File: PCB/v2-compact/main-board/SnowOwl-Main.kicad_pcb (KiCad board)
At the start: 4 copper layers, 70 x 100 mm, 30 parts, among them J1 STACK_2x10, J20 USB-C, J30 microSD, J31 TFT_SPI, SW1 BTN_UP, SW2 BTN_DN, SW3 BTN_L, SW4 BTN_R, SW5 BTN_OK, U20 ESP32-S3-WROOM-1-N8, U21 AP7361C-3.3, U22 USBLC6-2SC6

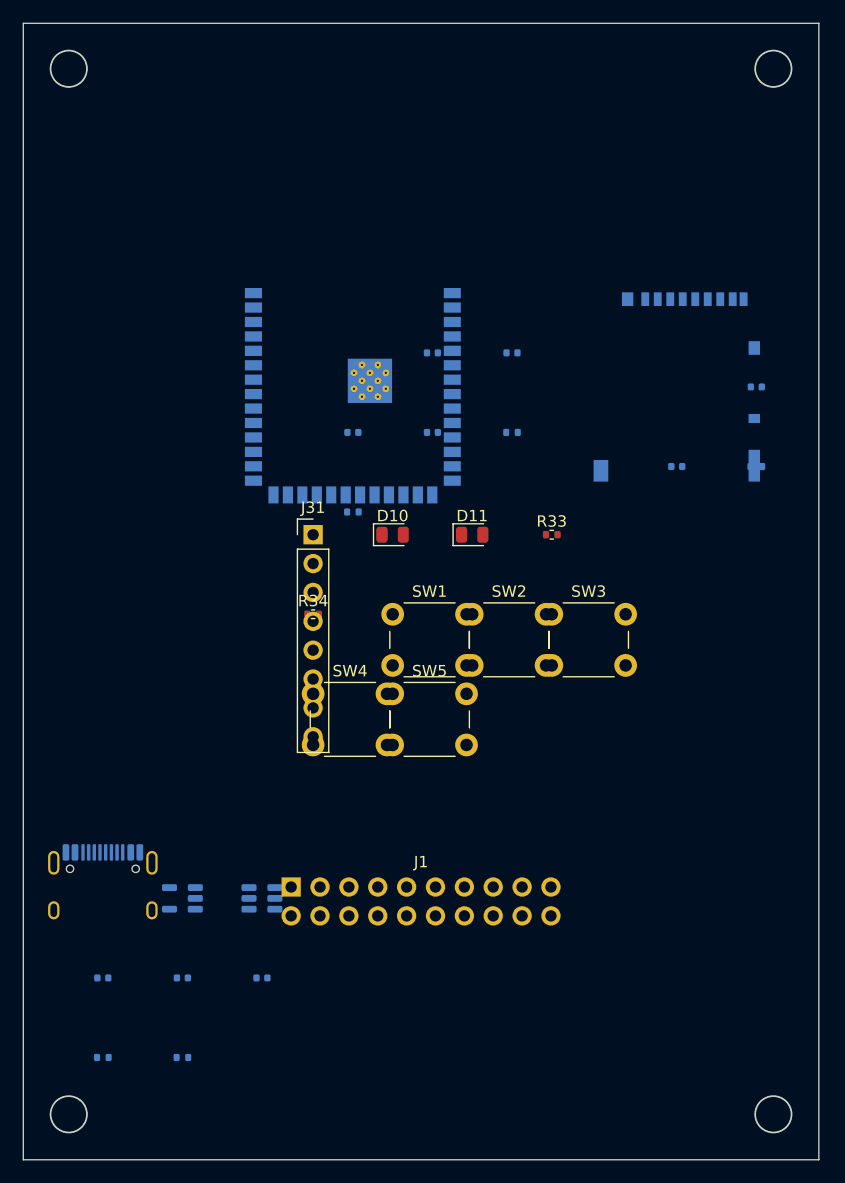
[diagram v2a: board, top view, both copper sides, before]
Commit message: PCB: intentional floorplan placement + 3D models + screen (both boards)
Reflow both boards to the PLACEMENT.md contract instead of a mechanical grid:
- Shield: radios north each behind its SMA, C5 (SPI master) centre with U.FL, the
  3 nRF24 on the back behind the QFN radios, MCP expander on the spine, PN532/flash/
  IR/iButton in their zones, J1 at the (53.57,106) datum, prog header off the crowded
  east edge. Main: pure-UI front (status LEDs, landscape TFT area, PlayStation D-pad
  SW1 up/SW2 down/SW3 left/SW4 right + SW5 select, J1 datum), all electronics on the
  back (S3 upper-centre with antenna to the edge, microSD east, power+USB-C south).
- Every support part anchored to the exact pin it shares a net with, then de-overlapped
  by spiralling out to the nearest clear spot inside the board, so decoupling hugs the
  power pins and crystals sit at the XTAL pins.
- Verified: 0 same-side courtyard overlaps, 0 cross-side through-hole collisions (new
  check that caught headers landing on back-side modules), every part in the outline.
- 3D models the renderer can find: C5 repointed to the Espressif model's absolute path,
  J1 given the KiCad 2x10 header body (rotated to match the horizontal pad layout).
- Draw the TFT display outline + label on the main front so the screen is visible.

Note: U9 (u-blox NEO) still renders as an outline - RF_GPS.3dshapes is absent from this
KiCad 3D pack; the footprint/courtyard are correct, only the cosmetic .step is missing.
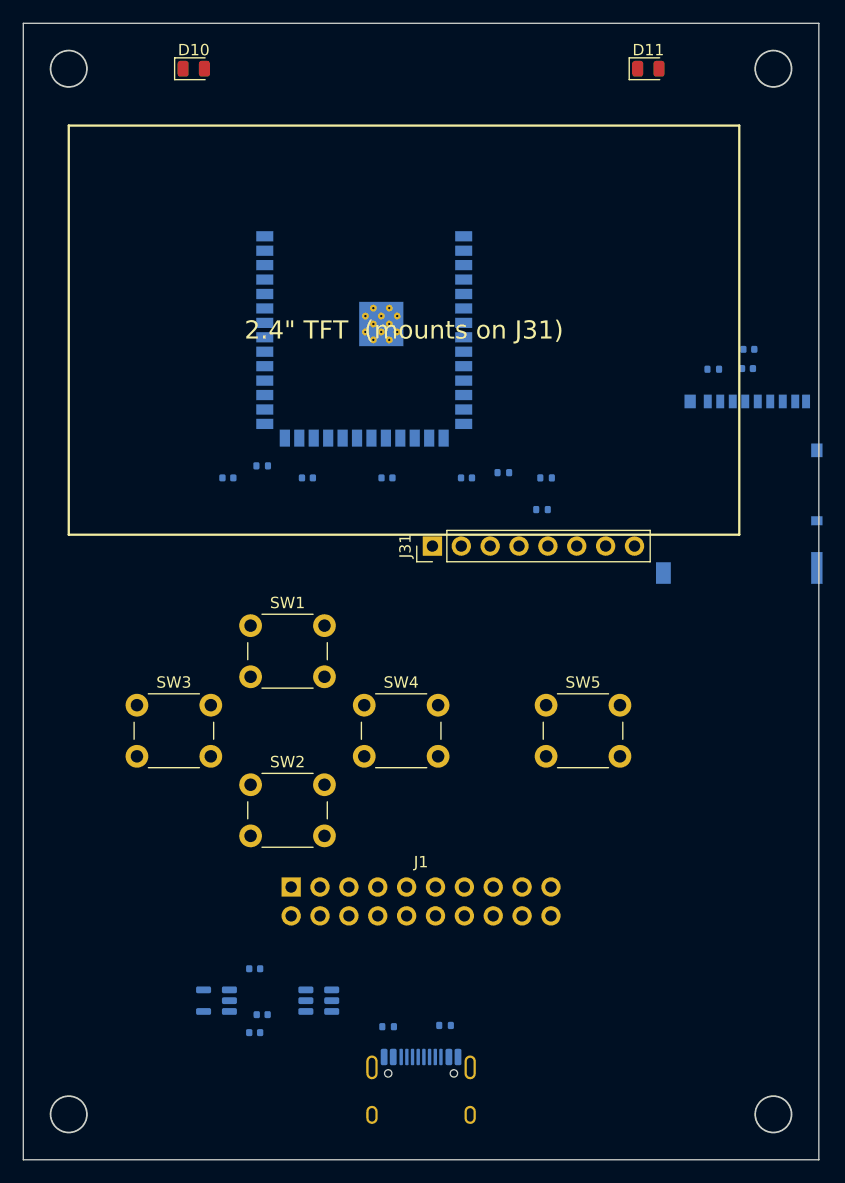
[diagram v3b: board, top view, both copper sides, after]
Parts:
- R33, R34: moved to B.Cu
- moved D10 44.6 mm to (45.0, 34.0)
- moved D11 43.8 mm to (85.0, 34.0)
- moved SW3 37.4 mm to (40.0, 90.0)
- moved J20 33.3 mm to (65.0, 125.0)
- moved R20 30.2 mm to (67.1, 118.2)
- moved SW2 24.6 mm to (50.0, 97.0)
- moved C30 21.1 mm to (48.0, 70.0)
- moved C31 21.1 mm to (55.0, 70.0)
- moved R34 20.9 mm to (72.2, 69.5), turned to 180 degrees
- moved R21 18.3 mm to (62.1, 118.3)
- moved SW5 13.5 mm to (76.0, 90.0)
- moved C20 13.4 mm to (50.4, 113.2)
- moved SW1 12.5 mm to (50.0, 83.0)
- moved C35 12.1 mm to (93.8, 58.7)
- moved J30 10.5 mm to (93.0, 71.0)
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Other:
- board text added: "2.4" TFT (mounts on J31)"
- board text removed: "TFT DISPLAY (landscape)"

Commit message: PCB: clear mounting-hole keepouts, pull off-board parts in, fix missing models
Second verification pass with a new thorough checker (mounting-hole clearance +
3D-model-FILE-exists, not just referenced):
- Mounting holes: add an M3 screw-head/standoff keepout to the placement engine so
  no support part lands near a corner hole (was dropping caps like C72 onto them).
  Move the parts that sat on holes: shield U9/U6 reflowed in the NE, prog header J40
  off the bottom-left hole; main S3 nudged clear of the NW hole.
- Off-board: J40 was hanging 4.5mm off the bottom edge (origin at pin 1) and J51 1.8mm
  off the east edge - both pulled fully inside the outline.
- Missing 3D model files (referenced but absent from this KiCad 3D pack): repoint U7's
  PN532 to the near-identical QFN-40 6x6 model, and the USB-C receptacles (J50/J20) to
  a GCT USB-C body, both present on disk.
- Result on both boards: 0 same-side overlaps, 0 cross-side hole collisions, 0 parts
  too close to a mounting hole, nothing hanging off the outline.

Still outstanding: only U9 (u-blox NEO) lacks a 3D model - RF_GPS.3dshapes is entirely
absent from this install's 3D pack (footprint/courtyard correct; needs the 3D pack).
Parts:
- moved C35 19.1 mm to (91.8, 77.7)
- moved J30 19.1 mm to (91.0, 90.0)
- moved R32 19.1 mm to (88.7, 79.4)
- moved C34 19.1 mm to (91.7, 79.4)
- moved R34 11.3 mm to (77.2, 79.7)
- moved R33 8.85 mm to (69.6, 79.2)
- moved C30 7.00 mm to (48.0, 77.0)
- moved C31 7.00 mm to (55.0, 77.0)
- moved C32 7.00 mm to (62.0, 77.0)
- moved C33 7.00 mm to (69.0, 77.0)
- moved R30 7.00 mm to (76.0, 77.0)
- moved R31 5.83 mm to (54.0, 73.9)
- moved U20 5.83 mm to (63.0, 59.0)
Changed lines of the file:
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@@
 	(footprint "C_0402_1005Metric"
 		(layer "B.Cu")
-		(at 93.84 58.69 180)
+		(at 91.84 77.69 180)
 		(descr "Capacitor SMD 0402 (1005 Metric), square (rectangular) end terminal, IPC-7351 nominal, (Body size source: IPC-SM-782 page 76, https://www.pcb-3d.com/wordpress/wp-content/uploads/ipc-sm-782a_amendment_1_and_2.pdf)")
 		(tags "capacitor")
@@
 	(footprint "C_0402_1005Metric"
 		(layer "B.Cu")
-		(at 69 70 180)
+		(at 69 77 180)
 		(descr "Capacitor SMD 0402 (1005 Metric), square (rectangular) end terminal, IPC-7351 nominal, (Body size source: IPC-SM-782 page 76, https://www.pcb-3d.com/wordpress/wp-content/uploads/ipc-sm-782a_amendment_1_and_2.pdf)")
 		(tags "capacitor")
@@
 	(footprint "microSD_HC_Hirose_DM3AT-SF-PEJM5"
 		(layer "B.Cu")
-		(at 93 71 180)
+		(at 91 90 180)
 		(descr "Micro SD, SMD, right-angle, push-pull (https://www.hirose.com/product/en/download_file/key_name/DM3AT-SF-PEJM5/category/Drawing%20(2D)/doc_file_id/44099/?file_category_id=6&item_id=06090031000&is_series=)")
 		(tags "Micro SD")
@@
 			(polygon
 				(pts
-					(xy 89.725 69.875) (xy 98.425 69.875) (xy 98.425 68.275) (xy 89.725 68.275)
+					(xy 87.725 88.875) (xy 96.425 88.875) (xy 96.425 87.275) (xy 87.725 87.275)
 				)
 			)
@@
 			(polygon
 				(pts
-					(xy 90.075 77.975) (xy 87.525 77.975) (xy 87.525 79.325) (xy 90.075 79.325)
+					(xy 88.075 96.975) (xy 85.525 96.975) (xy 85.525 98.325) (xy 88.075 98.325)
 				)
 			)
@@
 			(polygon
 				(pts
-					(xy 99.125 69.575) (xy 98.425 69.575) (xy 98.425 77.175) (xy 99.125 77.175)
+					(xy 97.125 88.575) (xy 96.425 88.575) (xy 96.425 96.175) (xy 97.125 96.175)
 				)
 			)
@@
 			(polygon
 				(pts
-					(xy 99.475 66.975) (xy 100.225 66.975) (xy 100.225 63.725) (xy 99.475 63.725)
+					(xy 97.475 85.975) (xy 98.225 85.975) (xy 98.225 82.725) (xy 97.475 82.725)
 				)
 			)
@@
 			(polygon
 				(pts
-					(xy 99.475 71.775) (xy 100.225 71.775) (xy 100.225 68.175) (xy 99.475 68.175)
+					(xy 97.475 90.775) (xy 98.225 90.775) (xy 98.225 87.175) (xy 97.475 87.175)
 				)
 			)
@@
 	(footprint "R_0402_1005Metric"
 		(layer "B.Cu")
-		(at 76 70 180)
+		(at 76 77 180)
 		(descr "Resistor SMD 0402 (1005 Metric), square (rectangular) end terminal, IPC-7351 nominal, (Body size source: IPC-SM-782 page 72, https://www.pcb-3d.com/wordpress/wp-content/uploads/ipc-sm-782a_amendment_1_and_2.pdf)")
 		(tags "resistor")
@@
 	(footprint "C_0402_1005Metric"
 		(layer "B.Cu")
-		(at 93.72 60.38 180)
+		(at 91.72 79.38 180)
 		(descr "Capacitor SMD 0402 (1005 Metric), square (rectangular) end terminal, IPC-7351 nominal, (Body size source: IPC-SM-782 page 76, https://www.pcb-3d.com/wordpress/wp-content/uploads/ipc-sm-782a_amendment_1_and_2.pdf)")
 		(tags "capacitor")
@@
 	(footprint "C_0402_1005Metric"
 		(layer "B.Cu")
-		(at 55 70 180)
+		(at 55 77 180)
 		(descr "Capacitor SMD 0402 (1005 Metric), square (rectangular) end terminal, IPC-7351 nominal, (Body size source: IPC-SM-782 page 76, https://www.pcb-3d.com/wordpress/wp-content/uploads/ipc-sm-782a_amendment_1_and_2.pdf)")
 		(tags "capacitor")
@@
 		)
 		(embedded_fonts no)
-		(model "${KICAD10_3DMODEL_DIR}/Connector_USB.3dshapes/USB_C_Receptacle_HRO_TYPE-C-31-M-12.step"
+		(model "C:/Users/artimi/AppData/Local/Programs/KiCad/10.0/share/kicad/3dmodels/Connector_USB.3dshapes/USB_C_Receptacle_GCT_USB4085.step"
 			(offset
 				(xyz 0 0 0)
@@
 	(footprint "R_0402_1005Metric"
 		(layer "B.Cu")
-		(at 90.71 60.44 180)
+		(at 88.71 79.44 180)
 		(descr "Resistor SMD 0402 (1005 Metric), square (rectangular) end terminal, IPC-7351 nominal, (Body size source: IPC-SM-782 page 72, https://www.pcb-3d.com/wordpress/wp-content/uploads/ipc-sm-782a_amendment_1_and_2.pdf)")
 		(tags "resistor")
@@
 	(footprint "R_0402_1005Metric"
 		(layer "B.Cu")
-		(at 75.64 72.79 180)
+		(at 69.59 79.25 180)
 		(descr "Resistor SMD 0402 (1005 Metric), square (rectangular) end terminal, IPC-7351 nominal, (Body size source: IPC-SM-782 page 72, https://www.pcb-3d.com/wordpress/wp-content/uploads/ipc-sm-782a_amendment_1_and_2.pdf)")
 		(tags "resistor")
@@
 	(footprint "C_0402_1005Metric"
 		(layer "B.Cu")
-		(at 62 70 180)
+		(at 62 77 180)
 		(descr "Capacitor SMD 0402 (1005 Metric), square (rectangular) end terminal, IPC-7351 nominal, (Body size source: IPC-SM-782 page 76, https://www.pcb-3d.com/wordpress/wp-content/uploads/ipc-sm-782a_amendment_1_and_2.pdf)")
 		(tags "capacitor")
@@
 	(footprint "R_0402_1005Metric"
 		(layer "B.Cu")
-		(at 72.24 69.54 180)
+		(at 77.16 79.69 180)
 		(descr "Resistor SMD 0402 (1005 Metric), square (rectangular) end terminal, IPC-7351 nominal, (Body size source: IPC-SM-782 page 72, https://www.pcb-3d.com/wordpress/wp-content/uploads/ipc-sm-782a_amendment_1_and_2.pdf)")
 		(tags "resistor")
@@
 	(footprint "C_0402_1005Metric"
 		(layer "B.Cu")
-		(at 48 70 180)
+		(at 48 77 180)
 		(descr "Capacitor SMD 0402 (1005 Metric), square (rectangular) end terminal, IPC-7351 nominal, (Body size source: IPC-SM-782 page 76, https://www.pcb-3d.com/wordpress/wp-content/uploads/ipc-sm-782a_amendment_1_and_2.pdf)")
 		(tags "capacitor")
@@
 	(footprint "R_0402_1005Metric"
 		(layer "B.Cu")
-		(at 51.02 68.94 180)
+		(at 54.02 73.94 180)
 		(descr "Resistor SMD 0402 (1005 Metric), square (rectangular) end terminal, IPC-7351 nominal, (Body size source: IPC-SM-782 page 72, https://www.pcb-3d.com/wordpress/wp-content/uploads/ipc-sm-782a_amendment_1_and_2.pdf)")
 		(tags "resistor")
@@
 	(footprint "ESP32-S3-WROOM-1"
 		(layer "B.Cu")
-		(at 60 54 180)
+		(at 63 59 180)
 		(descr "2.4 GHz Wi-Fi and Bluetooth module  https://www.espressif.com/sites/default/files/documentation/esp32-s3-wroom-1_wroom-1u_datasheet_en.pdf")
 		(tags "2.4 GHz Wi-Fi and Bluetooth module")
@@
 			(polygon
 				(pts
-					(xy 84 47.25) (xy 36 47.25) (xy 36 26.25) (xy 84 26.25)
+					(xy 87 52.25) (xy 39 52.25) (xy 39 31.25) (xy 87 31.25)
 				)
 			)

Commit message: PCB: orient microSD slots to the board edge, USB-C to the bottom-middle edge
Per the mechanical intent:
- microSD (J30 main, J51 shield): rotate to rot270 so the CARD SLOT opening faces the
  outside EAST edge - a card now slots straight in from the board edge instead of the slot
  pointing inward. Positioned so the opening sits at the edge.
- J50 (shield RV1106 USB-C): moved to the bottom-middle on the board edge with the opening
  facing SOUTH, matching J20 on the main board, so it's the charge + power/data port.
- Verified both USB-C receptacles carry power AND data: J20 = +5V/GND + USB_DP/DM + CC1/CC2;
  J50 = RV_5V + RV_USB_DP/DM + CC1/CC2.

Both boards still pass every check (0 overlaps, 0 cross-side hole collisions, 0 parts too
close to a mounting hole); the only edge flags are these connectors, which belong at the edge.
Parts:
- moved C35 22.3 mm to (72.7, 89.1)
- moved R32 20.8 mm to (72.8, 92.9)
- moved C34 18.1 mm to (75.4, 87.2)
- moved J30 5.00 mm to (86.0, 90.0), turned to -90 degrees
